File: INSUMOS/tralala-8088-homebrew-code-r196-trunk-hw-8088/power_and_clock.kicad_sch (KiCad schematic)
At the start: 37 parts, among them CON1 BARREL_JACK, P1 Conn_01x02_Male, SW1 RESET_8088, U1 74HCT00, U2 7805, U3 8284, Y1 6-30 MHz

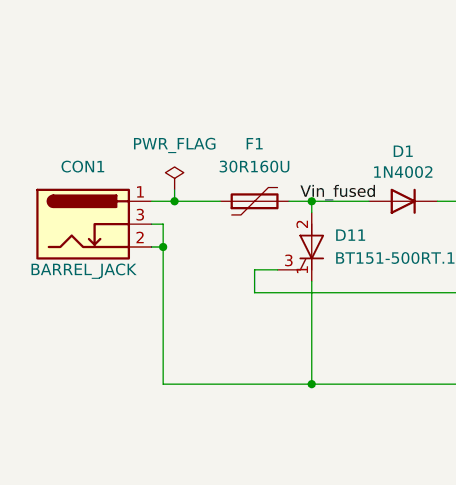
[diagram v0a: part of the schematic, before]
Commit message: Inicio da bios apos testes
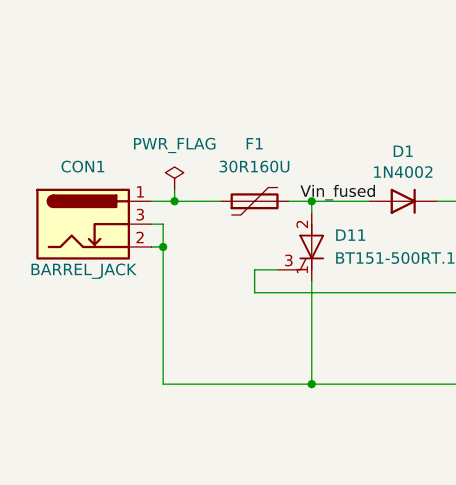
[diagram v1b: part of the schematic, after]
